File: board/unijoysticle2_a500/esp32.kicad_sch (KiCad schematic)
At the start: 17 parts, among them Q1 S8050, Q2 S8050, SW1 RESET, SW2 BOOT, U1 ESP32-WROOM-32E

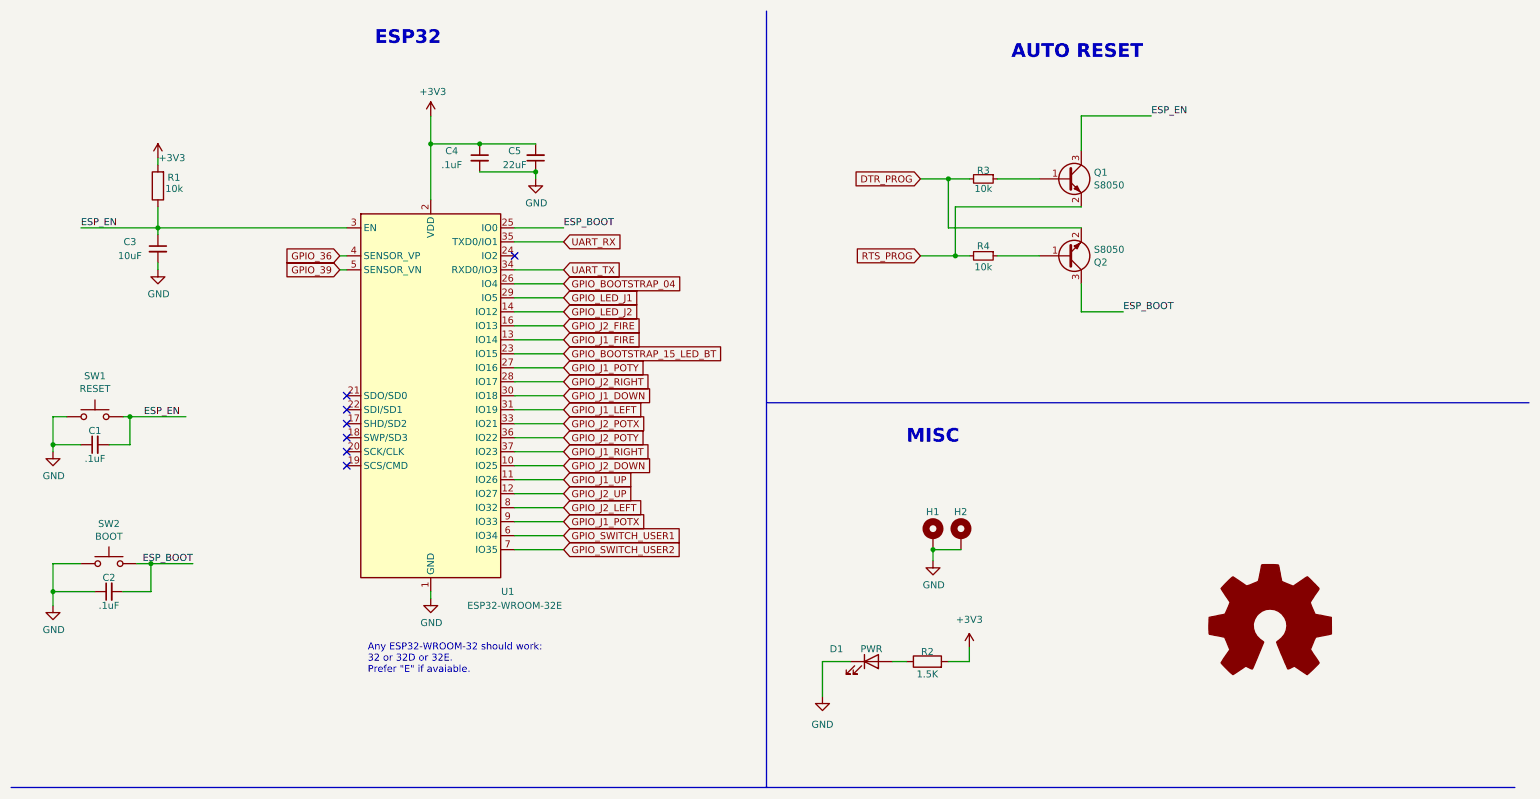
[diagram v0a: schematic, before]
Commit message: uni a500+: remove LSCS column
Values were outdated
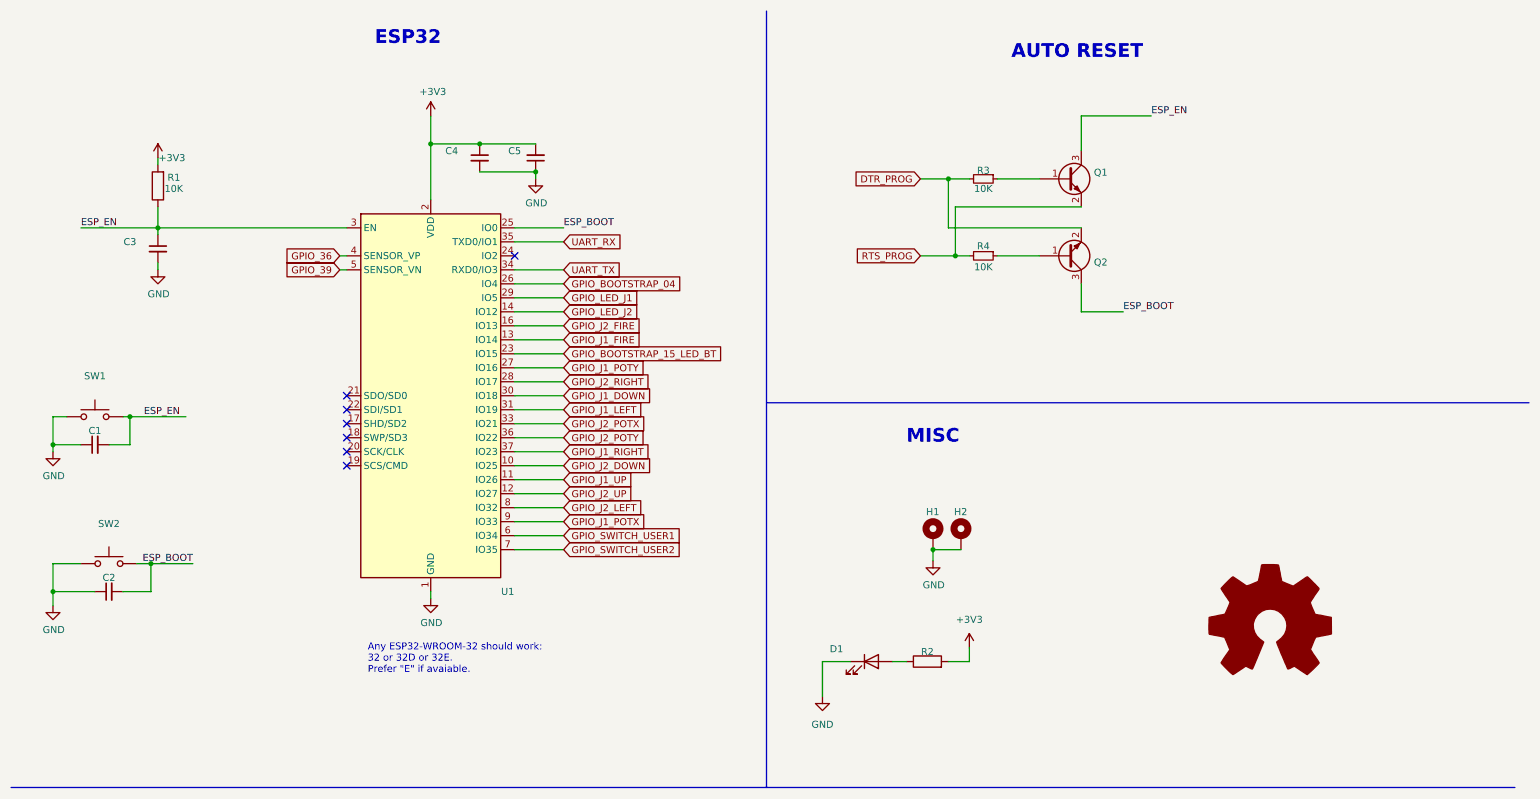
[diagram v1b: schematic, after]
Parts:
- C1, C2, C4: value .1uF -> (none); footprint Capacitor_SMD:C_0805_2012Metric_Pad1.18x1.45mm_HandSolder -> (none); LCSC C49678 -> (none)
- C3: value 10uF -> (none); footprint Capacitor_SMD:C_0805_2012Metric_Pad1.18x1.45mm_HandSolder -> (none); LCSC C15850 -> (none)
- C5: value 22uF -> (none); footprint Capacitor_SMD:C_0805_2012Metric_Pad1.18x1.45mm_HandSolder -> (none); LCSC C45783 -> (none)
- D1: value PWR -> (none); footprint LED_SMD:LED_0805_2012Metric_Pad1.15x1.40mm_HandSolder -> (none); LCSC C389525 -> (none)
- H1, H2: value MountingHole_Pad -> (none); footprint MountingHole:MountingHole_3.2mm_M3_Pad_Via -> (none)
- Q1, Q2: value S8050 -> (none); footprint Package_TO_SOT_SMD:SOT-23 -> (none); LCSC C2146 -> (none)
- R1, R3, R4: value 10k -> 10K; footprint Resistor_SMD:R_0805_2012Metric_Pad1.20x1.40mm_HandSolder -> (none); LCSC C17414 -> (none)
- R2: value 1.5K -> (none); footprint Resistor_SMD:R_0805_2012Metric_Pad1.20x1.40mm_HandSolder -> (none); LCSC C4310 -> (none)
- SW1: value RESET -> (none); footprint Button_Switch_THT:SW_Tactile_SPST_Angled_PTS645Vx39-2LFS -> (none)
- SW2: value BOOT -> (none); footprint Unijoysticle:SW_Push_1P1T_NO_5.1x5.1mm -> (none); LCSC C318884 -> (none)
- U1: value ESP32-WROOM-32E -> (none); footprint RF_Module:ESP32-WROOM-32 -> (none); LCSC C701341 -> (none)

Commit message: Uni 2 A500 Rev B:
- Cap 1500uF instead of 1000uF
- Use Resister 0 (R15) instead of JP2. Back resistor for JP2 2.2K
- LED resistors to be 2.2K
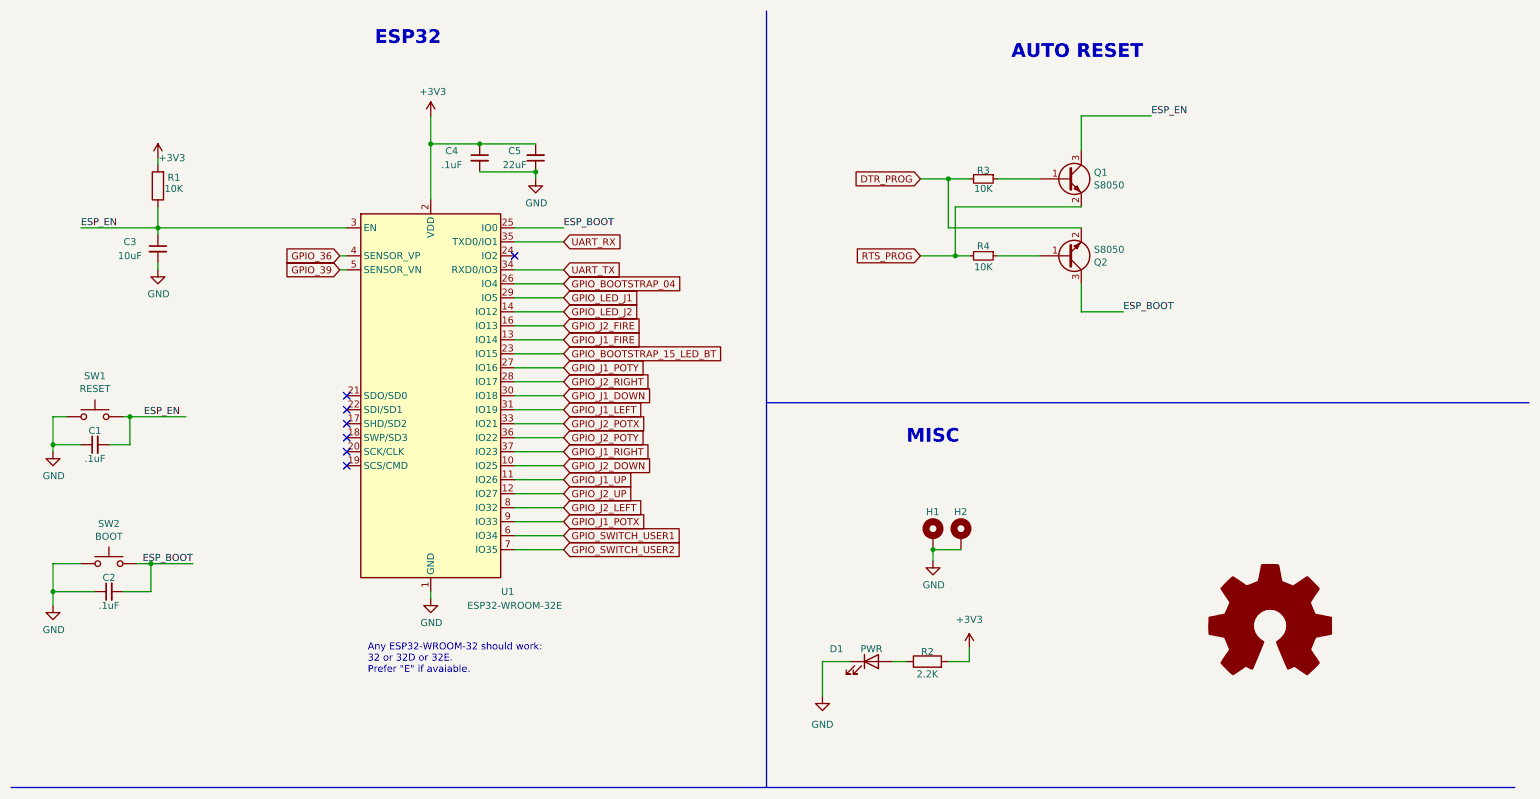
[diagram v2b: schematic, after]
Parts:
- C1, C2, C4: value (none) -> .1uF; footprint (none) -> Capacitor_SMD:C_0805_2012Metric_Pad1.18x1.45mm_HandSolder
- C3: value (none) -> 10uF; footprint (none) -> Capacitor_SMD:C_0805_2012Metric_Pad1.18x1.45mm_HandSolder
- C5: value (none) -> 22uF; footprint (none) -> Capacitor_SMD:C_0805_2012Metric_Pad1.18x1.45mm_HandSolder
- D1: value (none) -> PWR; footprint (none) -> LED_SMD:LED_0805_2012Metric_Pad1.15x1.40mm_HandSolder
- H1, H2: value (none) -> MountingHole_Pad; footprint (none) -> MountingHole:MountingHole_3.2mm_M3_Pad_Via
- Q1, Q2: value (none) -> S8050; footprint (none) -> Package_TO_SOT_SMD:SOT-23
- R1, R3, R4: footprint (none) -> Resistor_SMD:R_0805_2012Metric_Pad1.20x1.40mm_HandSolder
- R2: value (none) -> 2.2K; footprint (none) -> Resistor_SMD:R_0805_2012Metric_Pad1.20x1.40mm_HandSolder
- SW1: value (none) -> RESET; footprint (none) -> Button_Switch_THT:SW_Tactile_SPST_Angled_PTS645Vx39-2LFS
- SW2: value (none) -> BOOT; footprint (none) -> Unijoysticle:SW_Push_1P1T_NO_5.1x5.1mm
- U1: value (none) -> ESP32-WROOM-32E; footprint (none) -> RF_Module:ESP32-WROOM-32
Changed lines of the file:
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@@
   (title_block
     (title "Unijoysticle 2 A500")
-    (date "2022-04-25")
-    (rev "A")
+    (date "2022-05-15")
+    (rev "B")
     (company "Retro Moe")
   )
@@
     (in_bom yes) (on_board yes)
     (property "Reference" "U1" (id 0) (at 101.6 118.11 0))
-    (property "Value" "" (id 1) (at 102.87 120.65 0))
-    (property "Footprint" "" (id 2) (at 87.63 120.65 0)
+    (property "Value" "ESP32-WROOM-32E" (id 1) (at 102.87 120.65 0))
+    (property "Footprint" "RF_Module:ESP32-WROOM-32" (id 2) (at 87.63 120.65 0)
       (effects (font (size 1.27 1.27)) hide)
     )
@@
       (effects (font (size 1.27 1.27)) (justify left))
     )
-    (property "Footprint" "" (id 2) (at 39.878 44.45 90)
+    (property "Footprint" "Resistor_SMD:R_0805_2012Metric_Pad1.20x1.40mm_HandSolder" (id 2) (at 39.878 44.45 90)
       (effects (font (size 1.27 1.27)) hide)
     )
@@
     (in_bom yes) (on_board yes)
     (property "Reference" "SW1" (id 0) (at 26.67 78.9686 0))
-    (property "Value" "" (id 1) (at 26.67 81.28 0))
-    (property "Footprint" "" (id 2) (at 26.67 81.28 0)
+    (property "Value" "RESET" (id 1) (at 26.67 81.28 0))
+    (property "Footprint" "Button_Switch_THT:SW_Tactile_SPST_Angled_PTS645Vx39-2LFS" (id 2) (at 26.67 81.28 0)
       (effects (font (size 1.27 1.27)) hide)
     )
@@
       (effects (font (size 1.27 1.27)) (justify left))
     )
-    (property "Value" "" (id 1) (at 170.18 112.522 0)
-      (effects (font (size 1.27 1.27)) (justify left) hide)
-    )
-    (property "Footprint" "" (id 2) (at 178.816 107.95 0)
+    (property "Value" "MountingHole_Pad" (id 1) (at 170.18 112.522 0)
+      (effects (font (size 1.27 1.27)) (justify left) hide)
+    )
+    (property "Footprint" "MountingHole:MountingHole_3.2mm_M3_Pad_Via" (id 2) (at 178.816 107.95 0)
       (effects (font (size 1.27 1.27)) hide)
     )
@@
       (effects (font (size 1.27 1.27)) (justify left))
     )
-    (property "Value" "" (id 1) (at 175.006 112.522 0)
-      (effects (font (size 1.27 1.27)) (justify left) hide)
-    )
-    (property "Footprint" "" (id 2) (at 183.896 107.95 0)
+    (property "Value" "MountingHole_Pad" (id 1) (at 175.006 112.522 0)
+      (effects (font (size 1.27 1.27)) (justify left) hide)
+    )
+    (property "Footprint" "MountingHole:MountingHole_3.2mm_M3_Pad_Via" (id 2) (at 183.896 107.95 0)
       (effects (font (size 1.27 1.27)) hide)
     )
@@
     (in_bom yes) (on_board yes)
     (property "Reference" "C1" (id 0) (at 26.67 88.9 90))
-    (property "Value" "" (id 1) (at 26.67 93.98 90))
-    (property "Footprint" "" (id 2) (at 26.67 91.44 0)
+    (property "Value" ".1uF" (id 1) (at 26.67 93.98 90))
+    (property "Footprint" "Capacitor_SMD:C_0805_2012Metric_Pad1.18x1.45mm_HandSolder" (id 2) (at 26.67 91.44 0)
       (effects (font (size 1.27 1.27)) hide)
     )
@@
     (in_bom yes) (on_board yes)
     (property "Reference" "C3" (id 0) (at 33.02 54.61 0))
-    (property "Value" "" (id 1) (at 33.02 57.15 0))
-    (property "Footprint" "" (id 2) (at 38.1 55.88 0)
+    (property "Value" "10uF" (id 1) (at 33.02 57.15 0))
+    (property "Footprint" "Capacitor_SMD:C_0805_2012Metric_Pad1.18x1.45mm_HandSolder" (id 2) (at 38.1 55.88 0)
       (effects (font (size 1.27 1.27)) hide)
     )
@@
     (in_bom yes) (on_board yes)
     (property "Reference" "SW2" (id 0) (at 29.21 105.791 0))
-    (property "Value" "" (id 1) (at 29.21 108.1024 0))
-    (property "Footprint" "" (id 2) (at 29.21 107.95 0)
+    (property "Value" "BOOT" (id 1) (at 29.21 108.1024 0))
+    (property "Footprint" "Unijoysticle:SW_Push_1P1T_NO_5.1x5.1mm" (id 2) (at 29.21 107.95 0)
       (effects (font (size 1.27 1.27)) hide)
     )
@@
     (in_bom yes) (on_board yes)
     (property "Reference" "C2" (id 0) (at 29.21 115.57 90))
-    (property "Value" "" (id 1) (at 29.21 120.65 90))
-    (property "Footprint" "" (id 2) (at 29.21 118.11 0)
+    (property "Value" ".1uF" (id 1) (at 29.21 120.65 90))
+    (property "Footprint" "Capacitor_SMD:C_0805_2012Metric_Pad1.18x1.45mm_HandSolder" (id 2) (at 29.21 118.11 0)
       (effects (font (size 1.27 1.27)) hide)
     )
@@
     (in_bom yes) (on_board yes)
     (property "Reference" "C5" (id 0) (at 102.87 38.1 0))
-    (property "Value" "" (id 1) (at 102.87 40.64 0))
-    (property "Footprint" "" (id 2) (at 106.68 39.37 0)
+    (property "Value" "22uF" (id 1) (at 102.87 40.64 0))
+    (property "Footprint" "Capacitor_SMD:C_0805_2012Metric_Pad1.18x1.45mm_HandSolder" (id 2) (at 106.68 39.37 0)
       (effects (font (size 1.27 1.27)) hide)
     )
@@
     (in_bom yes) (on_board yes)
     (property "Reference" "C4" (id 0) (at 91.44 38.1 0))
-    (property "Value" "" (id 1) (at 91.44 40.64 0))
-    (property "Footprint" "" (id 2) (at 96.52 39.37 0)
+    (property "Value" ".1uF" (id 1) (at 91.44 40.64 0))
+    (property "Footprint" "Capacitor_SMD:C_0805_2012Metric_Pad1.18x1.45mm_HandSolder" (id 2) (at 96.52 39.37 0)
       (effects (font (size 1.27 1.27)) hide)
     )
@@
     (property "Reference" "R3" (id 0) (at 187.96 41.656 90))
     (property "Value" "10K" (id 1) (at 187.96 44.958 90))
-    (property "Footprint" "" (id 2) (at 187.96 43.18 0)
+    (property "Footprint" "Resistor_SMD:R_0805_2012Metric_Pad1.20x1.40mm_HandSolder" (id 2) (at 187.96 43.18 0)
       (effects (font (size 1.27 1.27)) hide)
     )
@@
     (in_bom yes) (on_board yes)
     (property "Reference" "D1" (id 0) (at 161.29 128.524 0))
-    (property "Value" "" (id 1) (at 167.64 128.524 0))
-    (property "Footprint" "" (id 2) (at 167.64 130.81 0)
+    (property "Value" "PWR" (id 1) (at 167.64 128.524 0))
+    (property "Footprint" "LED_SMD:LED_0805_2012Metric_Pad1.15x1.40mm_HandSolder" (id 2) (at 167.64 130.81 0)
       (effects (font (size 1.27 1.27)) hide)
     )
@@
     (property "Reference" "R4" (id 0) (at 187.96 55.372 90))
     (property "Value" "10K" (id 1) (at 187.96 59.182 90))
-    (property "Footprint" "" (id 2) (at 187.96 57.15 0)
+    (property "Footprint" "Resistor_SMD:R_0805_2012Metric_Pad1.20x1.40mm_HandSolder" (id 2) (at 187.96 57.15 0)
       (effects (font (size 1.27 1.27)) hide)
     )
@@
       (effects (font (size 1.27 1.27)) (justify left))
     )
-    (property "Value" "" (id 1) (at 208.026 56.007 0)
+    (property "Value" "S8050" (id 1) (at 208.026 56.007 0)
       (effects (font (size 1.27 1.27)) (justify left))
     )
-    (property "Footprint" "" (id 2) (at 208.28 59.69 0)
+    (property "Footprint" "Package_TO_SOT_SMD:SOT-23" (id 2) (at 208.28 59.69 0)
       (effects (font (size 1.27 1.27)) hide)
     )
@@
     (in_bom yes) (on_board yes)
     (property "Reference" "R2" (id 0) (at 177.8 129.032 90))
-    (property "Value" "" (id 1) (at 177.8 133.096 90))
-    (property "Footprint" "" (id 2) (at 177.8 132.588 90)
+    (property "Value" "2.2K" (id 1) (at 177.8 133.096 90))
+    (property "Footprint" "Resistor_SMD:R_0805_2012Metric_Pad1.20x1.40mm_HandSolder" (id 2) (at 177.8 132.588 90)
       (effects (font (size 1.27 1.27)) hide)
     )
@@
       (effects (font (size 1.27 1.27)) (justify left))
     )
-    (property "Value" "" (id 1) (at 208.026 44.323 0)
+    (property "Value" "S8050" (id 1) (at 208.026 44.323 0)
       (effects (font (size 1.27 1.27)) (justify left))
     )
-    (property "Footprint" "" (id 2) (at 208.28 40.64 0)
-      (effects (font (size 1.27 1.27)) hide)
-    )
+    (property "Footprint" "Package_TO_SOT_SMD:SOT-23" (id 2) (at 208.28 40.64 0)
+      (effects (font (size 1.27 1.27)) hide)
+    )

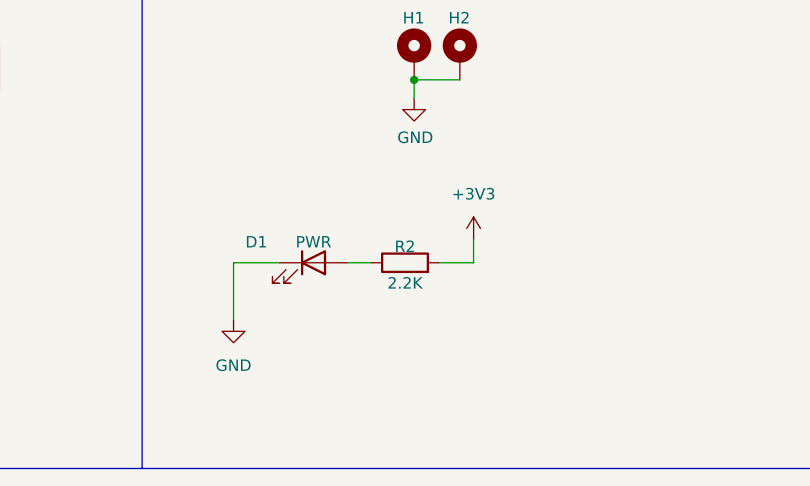
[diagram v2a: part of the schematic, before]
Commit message: uni2 a500: revert CH340 from 5V
Autoreset is driven by DTS/RTS.
But if DTS/RTS are not used (requires that CH340 is powered) then
autoreset doesn't work.
So, although we shouldn't power CH340 when it is powered from the Amiga,
since it consumes current, we need it for autoreset.

Besides, we don't gain much by not powering CH340. Only 0.02 amps
according to my measures.
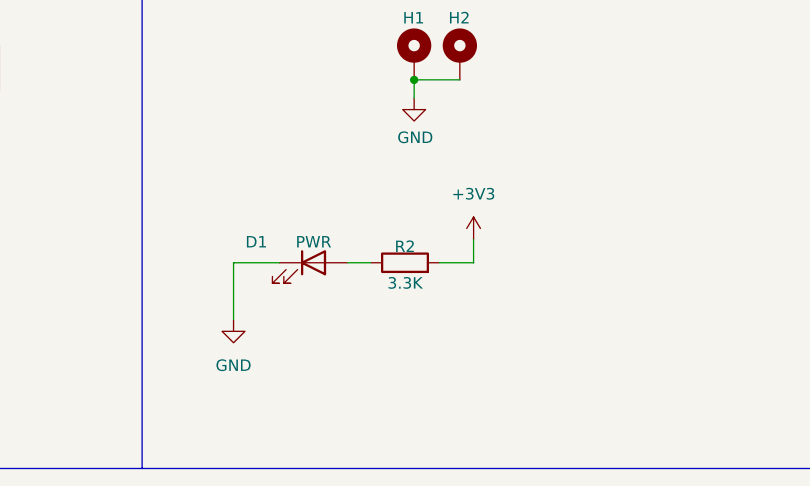
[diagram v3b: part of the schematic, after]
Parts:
- R2: value 2.2K -> 3.3K
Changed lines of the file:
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@@
     (in_bom yes) (on_board yes)
     (property "Reference" "R2" (id 0) (at 177.8 129.032 90))
-    (property "Value" "2.2K" (id 1) (at 177.8 133.096 90))
+    (property "Value" "3.3K" (id 1) (at 177.8 133.096 90))
     (property "Footprint" "Resistor_SMD:R_0805_2012Metric_Pad1.20x1.40mm_HandSolder" (id 2) (at 177.8 132.588 90)
       (effects (font (size 1.27 1.27)) hide)

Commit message: Uni2 A500: Change company name
from Retro Moe to Ricardo Quesada
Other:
- company: Retro Moe -> Ricardo Quesada
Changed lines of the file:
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@@
     (date "2022-05-15")
     (rev "B")
-    (company "Retro Moe")
+    (company "Ricardo Quesada")
   )
   (junction (at 36.83 113.03) (diameter 0) (color 0 0 0 0)
